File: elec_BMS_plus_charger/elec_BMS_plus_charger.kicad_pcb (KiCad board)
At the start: 2 copper layers, 20 x 20 mm, 18 parts, among them J1 JST SH, J7 JST SH, U1 AS5600L

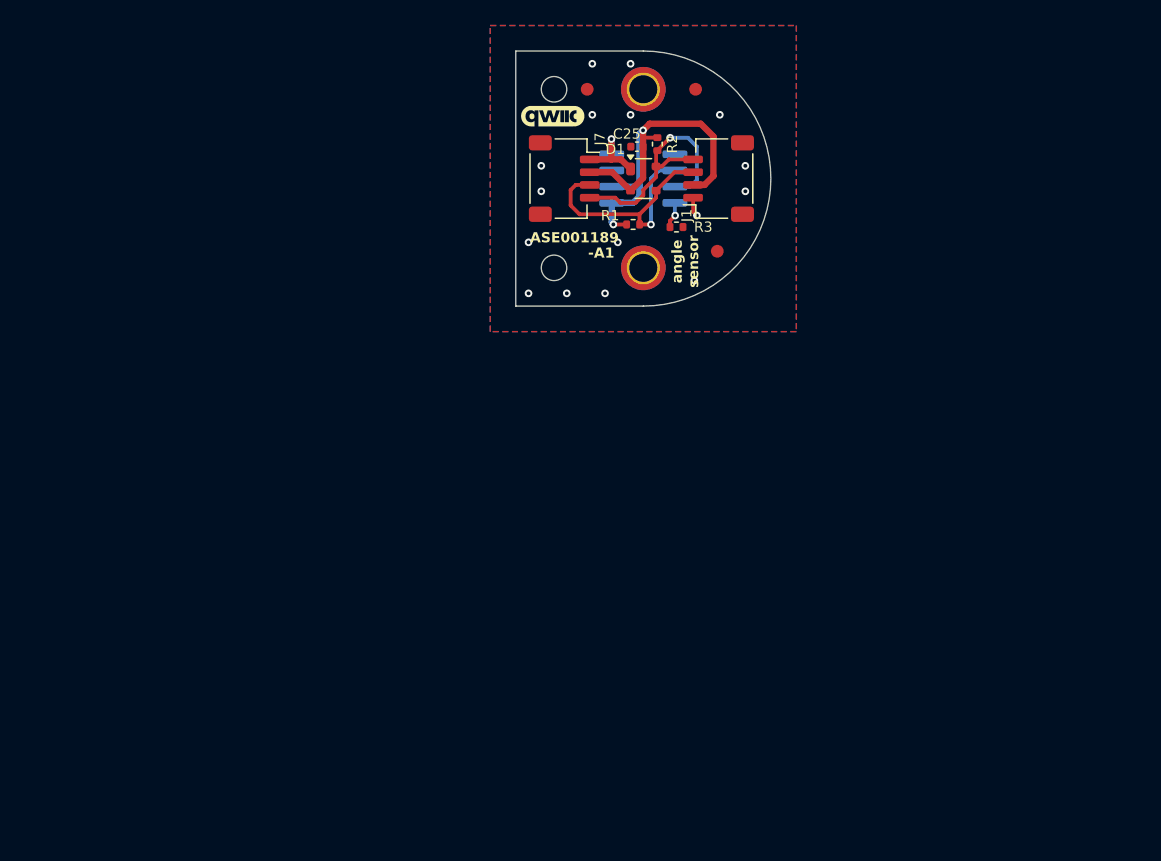
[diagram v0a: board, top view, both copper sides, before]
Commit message: [added] BMS/Charger
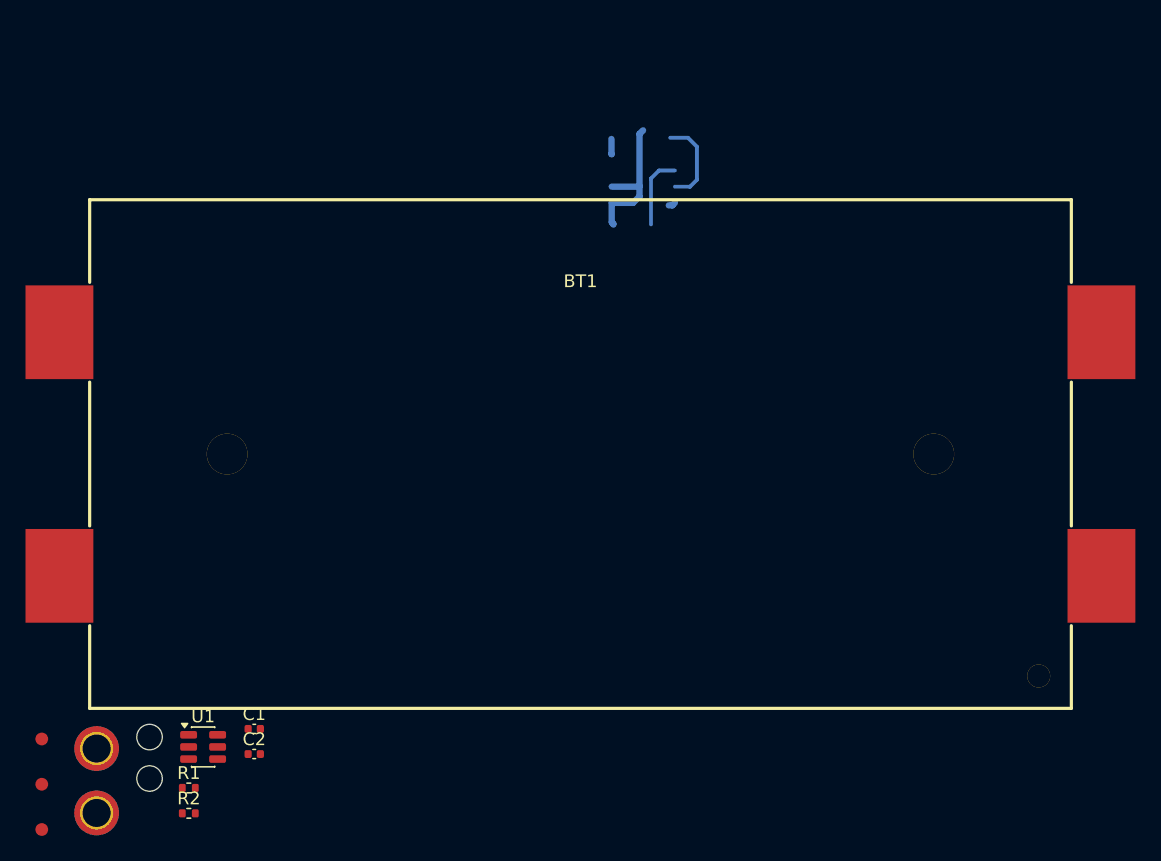
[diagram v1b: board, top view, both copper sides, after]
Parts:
- removed C25: 100n, Capacitor_SMD:C_0402_1005Metric
- removed D1: SP0503BAHT, Package_TO_SOT_SMD:SOT-143
- removed G1: qwiic_Logo, Library_Pollen:Logo_qwiic_5mm
- removed J1, J7: JST SH, Connector_JST:JST_SH_SM04B-SRSS-TB_1x04-1MP_P1.00mm_Horizontal
- removed R3: 0R, Resistor_SMD:R_0402_1005Metric
- added BT1: BH-18650-B1BA007, LCSC_parts_lib:BAT-SMD_BH-18650-B1BA007, F.Cu at (126.0, 71.2)
- added C1: 100n, Capacitor_SMD:C_0402_1005Metric, F.Cu at (100.4, 92.8)
- added C2: 100n, Capacitor_SMD:C_0402_1005Metric, F.Cu at (100.4, 94.8)
- R1, R2: value DNP-10k -> 330R
- U1: value AS5600L -> HY2120; footprint Package_SO:SOIC-8_3.9x4.9mm_P1.27mm -> Package_TO_SOT_SMD:SOT-23-6; moved to F.Cu
- moved FID1 72.3 mm to (83.7, 93.6)
- moved FID3 69.7 mm to (83.7, 100.7)
- moved FID2 69.3 mm to (83.7, 97.1)
- moved H4 67.2 mm to (88.0, 94.3)
- moved R2 64.1 mm to (95.3, 99.4), turned to 0 degrees
- moved H7 62.7 mm to (92.2, 96.7)
- moved H5 60.5 mm to (88.0, 99.4)
- moved U1 56.4 mm to (96.4, 94.2)
- moved R1 56.3 mm to (95.3, 97.4)
- moved H6 48.6 mm to (92.2, 93.4)
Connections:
- R1 pad 1: +3V3 -> +BATT
- R1 pad 2: Net-(J1-Pin_3) -> Net-(U1-Vdd)
- R2 pad 1: +3V3 -> Net-(BT1-Pad2)
- R2 pad 2: Net-(J1-Pin_4) -> Net-(U1-VC)
- U1 pad 1: +3V3 -> Net-(Q1-G)
- U1 pad 2: +3V3 -> Net-(Q2-G)
- U1 pad 3: unconnected-(U1-Out-Pad3) -> Net-(U1-CS)
- U1 pad 4: GND -> Net-(U1-VC)
- U1 pad 5: unconnected-(U1-PGO-Pad5) -> Net-(U1-Vdd)
- U1 pad 6: Net-(J1-Pin_3) -> Net-(U1-Vss)
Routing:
- net +3V3: track 35.2 -> 0.00 mm, vias 2 -> 0
- net (no net): track 0.00 -> 24.3 mm
- net Net-(J1-Pin_3): track 21.9 -> 0.00 mm, vias 1 -> 0
- net Net-(J1-Pin_4): track 20.0 -> 0.00 mm, vias 1 -> 0
- net GND: track 7.84 -> 1.76 mm, vias 17 -> 0
- net Net-(U1-Dir): track 2.08 -> 0.00 mm, vias 1 -> 0
- removed copper zone on B.Cu, net GND
- removed copper zone on F.Cu, net GND
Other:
- board outline removed
- board text removed: "!! Prévoir une place pour marquer l'adresse I2C du capteur d'angle"
- board text removed: "-A1"
- board text removed: "ASE001189"
- board text removed: "angle sensor"
